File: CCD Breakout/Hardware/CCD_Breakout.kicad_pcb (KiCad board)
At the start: 2 copper layers, 8 parts, among them J1 Conn_01x03_Pin, U1 ILX511

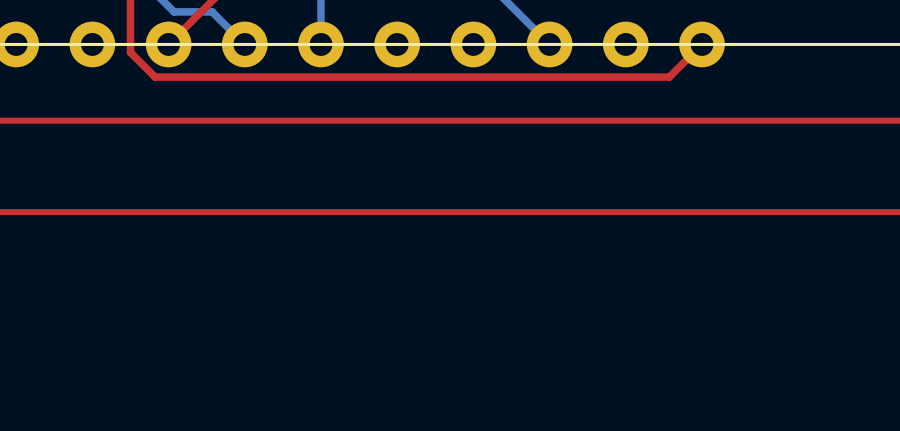
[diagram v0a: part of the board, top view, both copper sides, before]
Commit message: added signatures to all boards
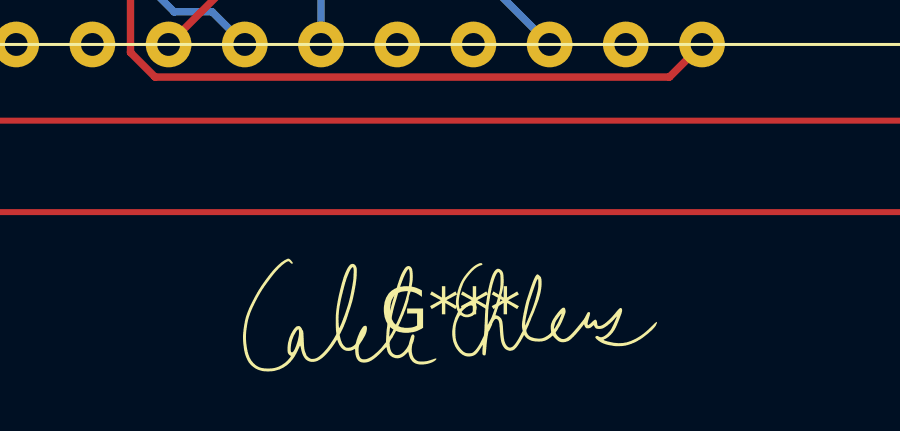
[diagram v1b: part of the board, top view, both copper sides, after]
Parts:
- added G***: LOGO, Signatures:Caleb_Ehlers_Signature_15mmx4.8mm, F.Cu at (72.9, 57.1)

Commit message: adjusted page sizes for all boards
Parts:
- Conn1: value Molex_SL_05 -> locked
- moved J1 16.3 mm to (73.4, 27.4)
- moved C1 16.3 mm to (85.5, 23.9)
- moved C3 16.3 mm to (84.7, 28.5)
- moved Conn1 16.3 mm to (56.9, 26.9)
- moved G*** 16.3 mm to (72.6, 40.9)
- moved V1 16.3 mm to (41.7, 26.9)
- moved V2 16.3 mm to (95.0, 26.9)
- moved C2 16.3 mm to (85.5, 26.4)
- moved U1 16.3 mm to (47.5, 22.0)

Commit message: finish ccd board
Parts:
- C3: footprint Capacitor_SMD:C_0201_0603Metric_Pad0.64x0.40mm_HandSolder -> Capacitor_SMD:C_0603_1608Metric_Pad1.08x0.95mm_HandSolder
- G***: moved to B.Cu
- moved G*** 21.1 mm to (88.4, 26.9), turned to -90 degrees
- moved C2 3.07 mm to (84.2, 29.2)
- moved C3 1.70 mm to (84.2, 26.9)
- moved C1 1.47 mm to (84.2, 24.6)
- moved Conn1 0.51 mm to (56.9, 26.4)
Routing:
- net øROG: track 25.2 -> 21.4 mm
- net +5V: track 69.1 -> 65.9 mm
- net Vout: track 13.7 -> 11.2 mm, vias 0 -> 1
- net Net-(U1-VGG): track 19.6 -> 18.7 mm
- net SHSW: vias 0 -> 1
- net GND: vias 2 -> 0
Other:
- board outline added: 63.5 x 15.2 mm
- board text added: "CCD Breakout"
